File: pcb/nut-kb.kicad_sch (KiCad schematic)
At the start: 150 parts, among them J1 Battery Connector, J2 E Ink Display, J3 E Ink Display, J4 Battery Connector, SW1 SW_Push, SW2 SW_SPST, SW3 SW_Push, SW4 SW_SPST, U1 nice_nano_left, U2 nice_nano_right

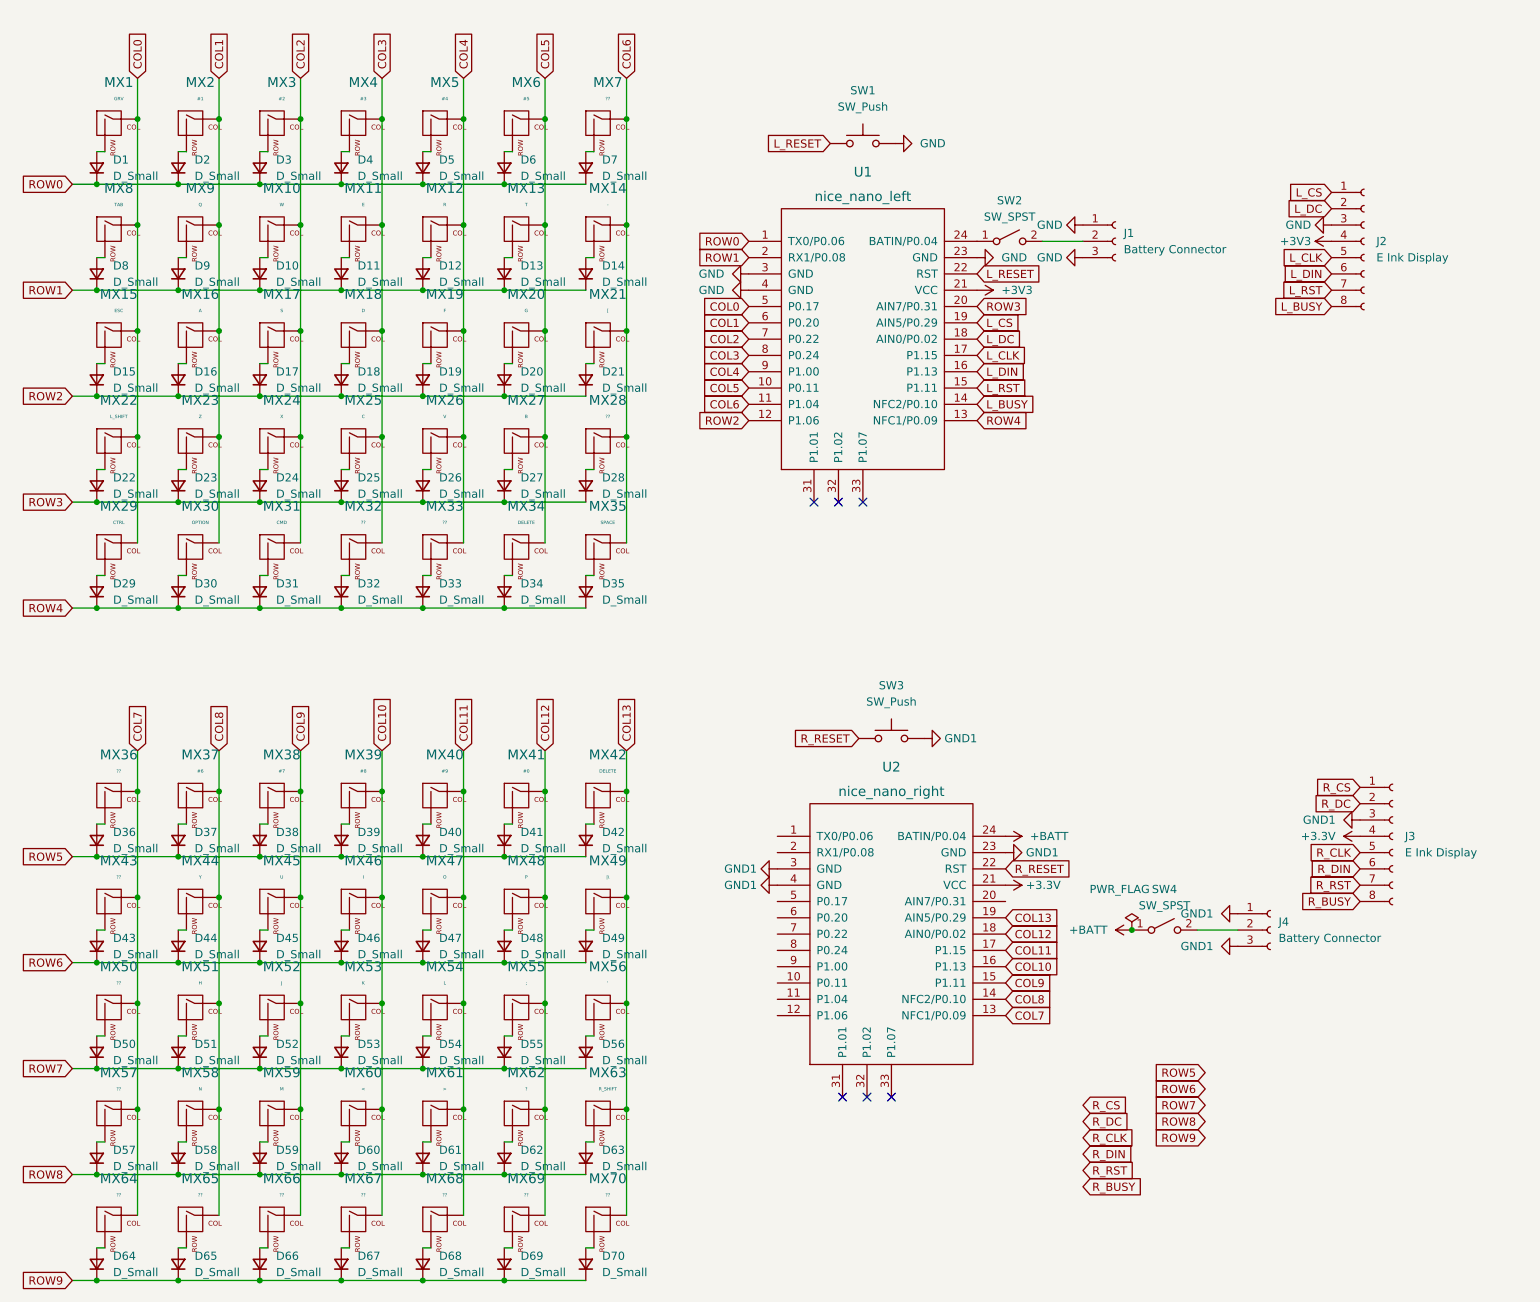
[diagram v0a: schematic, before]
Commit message: [pcb] finish keyboard
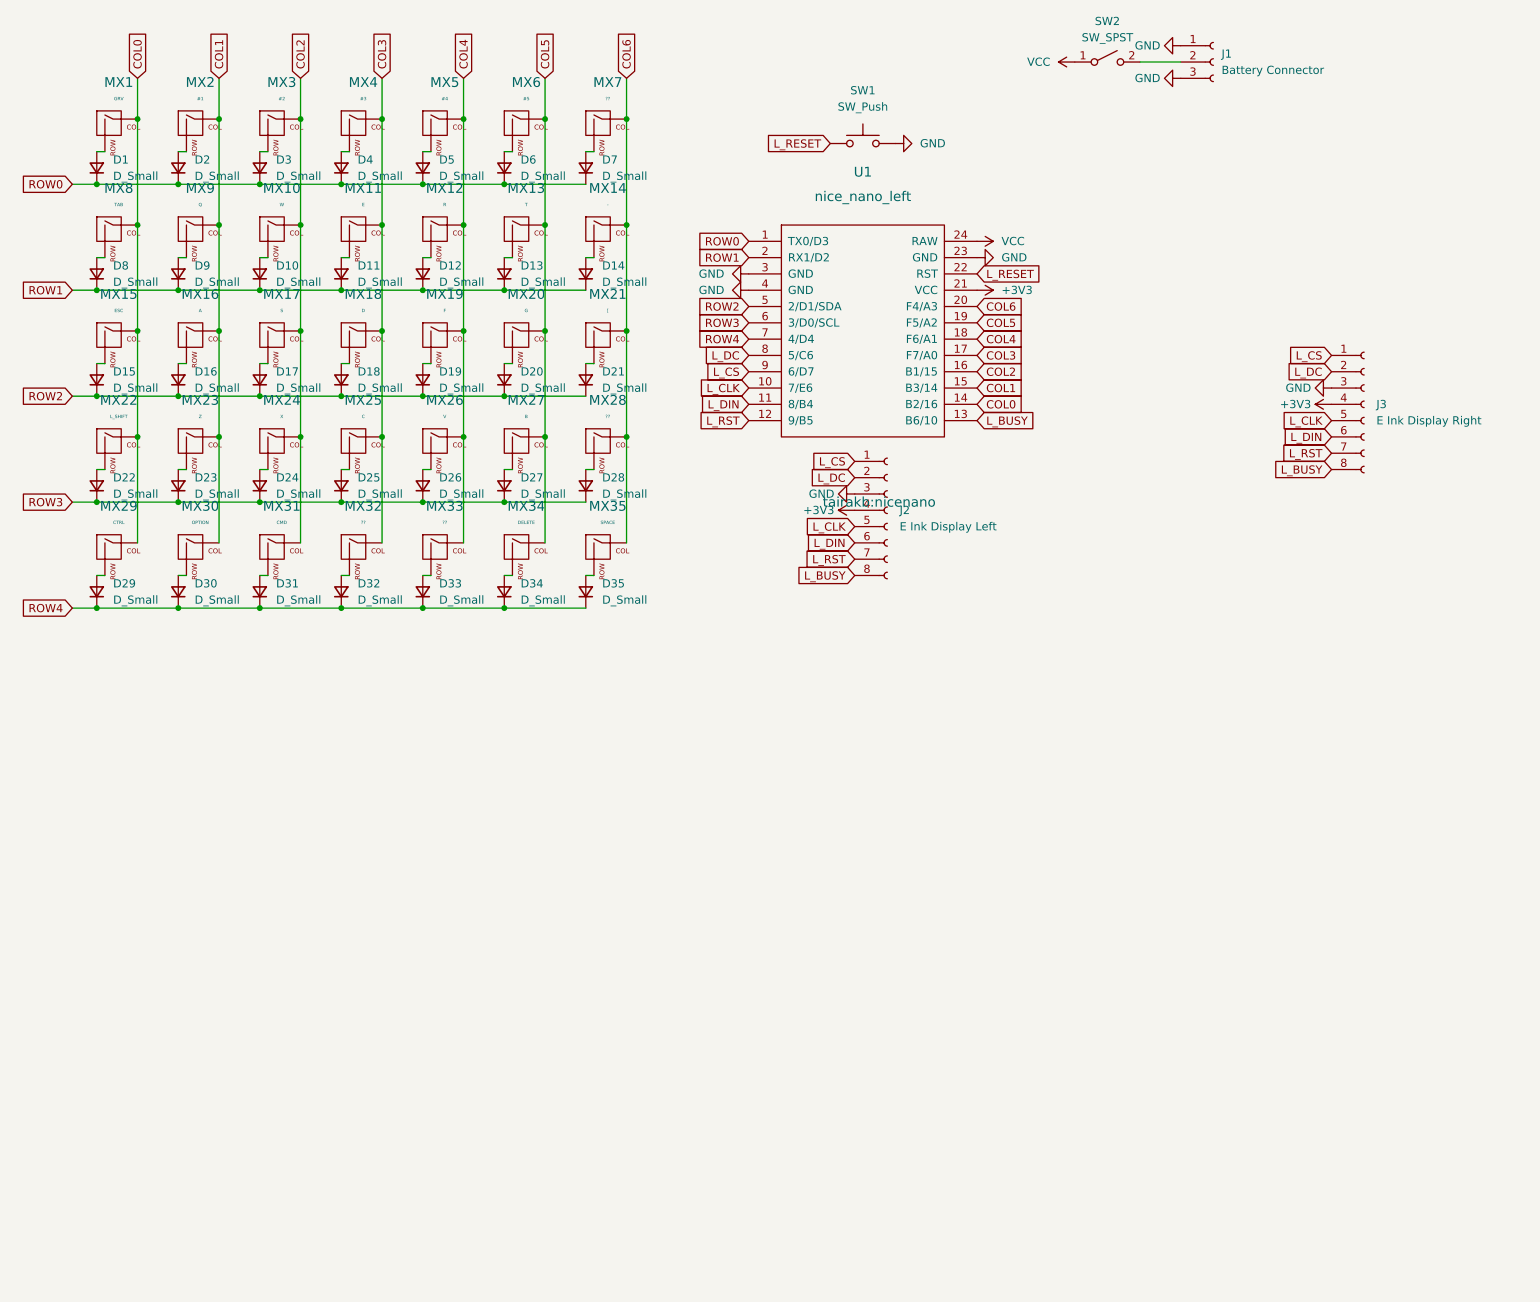
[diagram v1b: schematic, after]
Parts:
- removed D36, D37, D38, D39, D40, D41, D42, D43, D44, D45, D46, D47, D48, D49, D50, D51, D52, D53, D54, D55, D56, D57, D58, D59, D60, D61, D62, D63, D64, D65, D66, D67, D68, D69, D70: D_Small, Diode_SMD:D_SOD-123, symbol Device:D_Small
- removed J4: Battery Connector, Connector_JST:JST_PH_B3B-PH-K_1x03_P2.00mm_Vertical, symbol Connector:Conn_01x03_Female
- removed MX36, MX43, MX50, MX57, MX66, MX67, MX68, MX69, MX70: ??, Switch_Keyboard_Kailh:SW_Kailh_Choc_V1_1.00u, symbol MX_Alps_Hybrid:MX-NoLED
- removed MX37: #6, Switch_Keyboard_Kailh:SW_Kailh_Choc_V1_1.00u, symbol MX_Alps_Hybrid:MX-NoLED
- removed MX38: #7, Switch_Keyboard_Kailh:SW_Kailh_Choc_V1_1.00u, symbol MX_Alps_Hybrid:MX-NoLED
- removed MX39: #8, Switch_Keyboard_Kailh:SW_Kailh_Choc_V1_1.00u, symbol MX_Alps_Hybrid:MX-NoLED
- removed MX40: #9, Switch_Keyboard_Kailh:SW_Kailh_Choc_V1_1.00u, symbol MX_Alps_Hybrid:MX-NoLED
- removed MX41: #0, Switch_Keyboard_Kailh:SW_Kailh_Choc_V1_1.00u, symbol MX_Alps_Hybrid:MX-NoLED
- removed MX42: DELETE, Switch_Keyboard_Kailh:SW_Kailh_Choc_V1_1.00u, symbol MX_Alps_Hybrid:MX-NoLED
- removed MX44: Y, Switch_Keyboard_Kailh:SW_Kailh_Choc_V1_1.00u, symbol MX_Alps_Hybrid:MX-NoLED
- removed MX45: U, Switch_Keyboard_Kailh:SW_Kailh_Choc_V1_1.00u, symbol MX_Alps_Hybrid:MX-NoLED
- removed MX46: I, Switch_Keyboard_Kailh:SW_Kailh_Choc_V1_1.00u, symbol MX_Alps_Hybrid:MX-NoLED
- removed MX47: O, Switch_Keyboard_Kailh:SW_Kailh_Choc_V1_1.00u, symbol MX_Alps_Hybrid:MX-NoLED
- removed MX48: P, Switch_Keyboard_Kailh:SW_Kailh_Choc_V1_1.00u, symbol MX_Alps_Hybrid:MX-NoLED
- removed MX49: |\, Switch_Keyboard_Kailh:SW_Kailh_Choc_V1_1.00u, symbol MX_Alps_Hybrid:MX-NoLED
- removed MX51: H, Switch_Keyboard_Kailh:SW_Kailh_Choc_V1_1.00u, symbol MX_Alps_Hybrid:MX-NoLED
- removed MX52: J, Switch_Keyboard_Kailh:SW_Kailh_Choc_V1_1.00u, symbol MX_Alps_Hybrid:MX-NoLED
- removed MX53: K, Switch_Keyboard_Kailh:SW_Kailh_Choc_V1_1.00u, symbol MX_Alps_Hybrid:MX-NoLED
- removed MX54: L, Switch_Keyboard_Kailh:SW_Kailh_Choc_V1_1.00u, symbol MX_Alps_Hybrid:MX-NoLED
- removed MX55: ;, Switch_Keyboard_Kailh:SW_Kailh_Choc_V1_1.00u, symbol MX_Alps_Hybrid:MX-NoLED
- removed MX56: ', Switch_Keyboard_Kailh:SW_Kailh_Choc_V1_1.00u, symbol MX_Alps_Hybrid:MX-NoLED
- removed MX58: N, Switch_Keyboard_Kailh:SW_Kailh_Choc_V1_1.00u, symbol MX_Alps_Hybrid:MX-NoLED
- removed MX59: M, Switch_Keyboard_Kailh:SW_Kailh_Choc_V1_1.00u, symbol MX_Alps_Hybrid:MX-NoLED
- removed MX60: <, Switch_Keyboard_Kailh:SW_Kailh_Choc_V1_1.00u, symbol MX_Alps_Hybrid:MX-NoLED
- removed MX61: >, Switch_Keyboard_Kailh:SW_Kailh_Choc_V1_1.00u, symbol MX_Alps_Hybrid:MX-NoLED
- removed MX62: ?, Switch_Keyboard_Kailh:SW_Kailh_Choc_V1_1.00u, symbol MX_Alps_Hybrid:MX-NoLED
- removed MX63: R_SHIFT, Switch_Keyboard_Kailh:SW_Kailh_Choc_V1_1.00u, symbol MX_Alps_Hybrid:MX-NoLED
- removed MX64, MX65: ??, Switch_Keyboard_Kailh:SW_Kailh_Choc_V1_2.00u_90deg, symbol MX_Alps_Hybrid:MX-NoLED
- removed SW3: SW_Push, Button_Switch_THT:SW_PUSH_6mm, symbol Switch:SW_Push
- removed SW4: SW_SPST, Button_Switch_THT:SW_DIP_SPSTx01_Slide_6.7x4.1mm_W7.62mm_P2.54mm_LowProfile, symbol Switch:SW_SPST
- removed U2: nice_nano_right, nice-nano-kicad:nice_nano, symbol nice_nano:nice_nano
- J2: value E Ink Display -> E Ink Display Left
- J3: value E Ink Display -> E Ink Display Right
- MX1, MX10, MX11, MX12, MX13, MX14, MX15, MX16, MX17, MX18, MX19, MX2, MX20, MX21, MX22, MX23, MX24, MX25, MX26, MX27, MX28, MX29, MX3, MX30, MX31, MX32, MX33, MX4, MX5, MX6, MX7, MX8, MX9: footprint Switch_Keyboard_Kailh:SW_Kailh_Choc_V1_1.00u -> keyswitches:SW_PG1350_reversible
- MX34, MX35: footprint Switch_Keyboard_Kailh:SW_Kailh_Choc_V1_2.00u_90deg -> keyswitches:SW_PG1350_reversible
- U1: footprint nice-nano-kicad:nice_nano -> tairakb:nicenano; symbol nice_nano:nice_nano -> tairakb:ProMicro
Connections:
- net GND1 is gone; now on net GND: J3.3 (Pin_3)
- net R_BUSY is gone; now on net L_BUSY: J3.8 (Pin_8)
- net R_CLK is gone; now on net L_CLK: J3.5 (Pin_5)
- net R_CS is gone; now on net L_CS: J3.1 (asdf)
- net R_DC is gone; now on net L_DC: J3.2 (Pin_2)
- net R_DIN is gone; now on net L_DIN: J3.6 (Pin_6)
- net R_RST is gone; now on net L_RST: J3.7 (Pin_7)
- net COL0: now also U1.14 (B2/16); no longer U1.5 (P0.17)
- net COL1: now also U1.15 (B3/14); no longer U1.6 (P0.20)
- net COL2: now also U1.16 (B1/15); no longer U1.7 (P0.22)
- net COL3: now also U1.17 (F7/A0); no longer U1.8 (P0.24)
- net COL4: now also U1.18 (F6/A1); no longer U1.9 (P1.00)
- net COL5: now also U1.19 (F5/A2); no longer U1.10 (P0.11)
- net COL6: now also U1.20 (F4/A3); no longer U1.11 (P1.04)
- net L_BUSY: now also U1.13 (B6/10); no longer U1.14 (NFC2/P0.10)
- net L_CLK: now also U1.10 (7/E6); no longer U1.17 (P1.15)
- net L_CS: now also U1.9 (6/D7); no longer U1.19 (AIN5/P0.29)
- net L_DC: now also U1.8 (5/C6); no longer U1.18 (AIN0/P0.02)
- net L_DIN: now also U1.11 (8/B4); no longer U1.16 (P1.13)
- net L_RST: now also U1.12 (9/B5); no longer U1.15 (P1.11)
- net ROW2: now also U1.5 (2/D1/SDA); no longer U1.12 (P1.06)
- net ROW3: now also U1.6 (3/D0/SCL); no longer U1.20 (AIN7/P0.31)
- net ROW4: now also U1.7 (4/D4); no longer U1.13 (NFC1/P0.09)
- net VCC: now reaches SW2.1 (A), U1.24 (RAW)
- no-connect marks 6 -> 0
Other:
- moved on the sheet: J1, J2, SW2
